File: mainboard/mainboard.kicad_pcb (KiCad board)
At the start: 2 copper layers, 94 parts, among them J1 CV-A, J2 In-A, J3 In-AB, J4 In-B, J5 Eurorack_Power, J6 CV-B, J7 Out-A, J8 Out-AB, J9 Out-B, Q1 BC547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

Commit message: Panel and trace corrections
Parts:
- added R50: 47k, Resistor_THT:R_Axial_DIN0204_L3.6mm_D1.6mm_P7.62mm_Horizontal, F.Cu at (68.5, 38.0)
- moved R37 174.9 mm to (18.5, 54.7), turned to -90 degrees
- moved R47 169.9 mm to (2.44, 39.8)
- moved R20 168.1 mm to (26.0, 54.7), turned to -90 degrees
- moved Q2 165.8 mm to (38.2, 34.0), turned to 90 degrees
- moved C9 165.1 mm to (39.2, 46.8), turned to 90 degrees
- moved Q4 162.0 mm to (32.2, 31.5), turned to -90 degrees
- moved R24 161.6 mm to (31.2, 39.5)
- moved R3 159.5 mm to (26.0, 20.0), turned to 180 degrees
- moved R26 159.4 mm to (18.4, 83.8)
- moved Q3 157.8 mm to (36.8, 17.0), turned to 90 degrees
- moved C10 155.2 mm to (40.8, 12.8), turned to -90 degrees
- moved R8 153.9 mm to (30.0, 20.5), turned to -90 degrees
- moved R30 153.5 mm to (30.0, 69.5), turned to 90 degrees
- moved C14 152.6 mm to (13.2, 86.8), turned to -90 degrees
- moved C6 149.6 mm to (39.2, 6.75), turned to 90 degrees
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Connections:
- R13 pad 2: Net-(R10-Pad1) -> Net-(R13-Pad2)
- R5 pad 2: Net-(R10-Pad1) -> Net-(R13-Pad2)
- R9 pad 1: Net-(R10-Pad1) -> Net-(R13-Pad2)
- U1 pad 2: unconnected-(U1-Pad2) -> GND
- U2 pad 12: MIDO1 -> Net-(RV3-Pad2)
- U2 pad 13: Net-(C10-Pad1) -> Net-(R13-Pad2)
- U2 pad 14: Net-(C10-Pad2) -> Net-(R13-Pad1)
- U2 pad 5: Net-(RV3-Pad2) -> MIDO1
- U2 pad 6: Net-(R10-Pad1) -> Net-(C10-Pad1)
- U2 pad 7: Net-(R13-Pad1) -> Net-(C10-Pad2)
- U3 pad 12: MIDO2 -> Net-(RV4-Pad2)
- U3 pad 13: Net-(C11-Pad1) -> Net-(R10-Pad1)
- U3 pad 14: Net-(C11-Pad2) -> Net-(R14-Pad1)
- U3 pad 5: Net-(RV4-Pad2) -> MIDO2
- U3 pad 6: Net-(R10-Pad1) -> Net-(C11-Pad1)
- U3 pad 7: Net-(R14-Pad1) -> Net-(C11-Pad2)
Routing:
- net GND: track 0.00 -> 463.9 mm, vias 0 -> 2
- net +9V: track 0.00 -> 297.5 mm, vias 0 -> 1
- net MIDO2: track 0.00 -> 101.9 mm, vias 0 -> 1
- net MIDO1: track 0.00 -> 98.1 mm
- net Net-(C11-Pad2): track 0.00 -> 93.9 mm, vias 0 -> 2
- net Net-(R16-Pad1): track 0.00 -> 93.5 mm
- net Net-(R33-Pad1): track 0.00 -> 77.2 mm
- net Net-(RV4-Pad2): track 0.00 -> 74.5 mm, vias 0 -> 1
- net Net-(C10-Pad2): track 0.00 -> 74.3 mm, vias 0 -> 1
- net Net-(C11-Pad1): track 0.00 -> 64.5 mm, vias 0 -> 1
- net Net-(C7-Pad1): track 0.00 -> 64.0 mm
- net Net-(R34-Pad1): track 0.00 -> 62.6 mm
- net Net-(C8-Pad1): track 0.00 -> 62.0 mm, vias 0 -> 1
- net Net-(R17-Pad1): track 0.00 -> 60.6 mm
- net Net-(C10-Pad1): track 0.00 -> 58.3 mm
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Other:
- board outline added: 70 x 100 mm
- board text added: "circuit: Ciat-Lonbarde pcb: Neil Massey"
- board text added: "panel components other side!"
- board text added: "panel components this side!"
- board text added: "thanks: Josh Rodriguez, T.Johns"

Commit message: Panel tweaks
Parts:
- moved J1 0.25 mm to (64.0, 28.5)
- moved J2 0.25 mm to (64.0, 6.50)
- moved J3 0.25 mm to (64.0, 50.0)
- moved J4 0.25 mm to (64.0, 91.0)
- moved J6 0.25 mm to (64.0, 70.5)
- moved J7 0.25 mm to (6.00, 6.50)
- moved J8 0.25 mm to (6.00, 50.0)
- moved J9 0.25 mm to (6.00, 91.0)
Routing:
- net GND: track 463.9 -> 464.5 mm

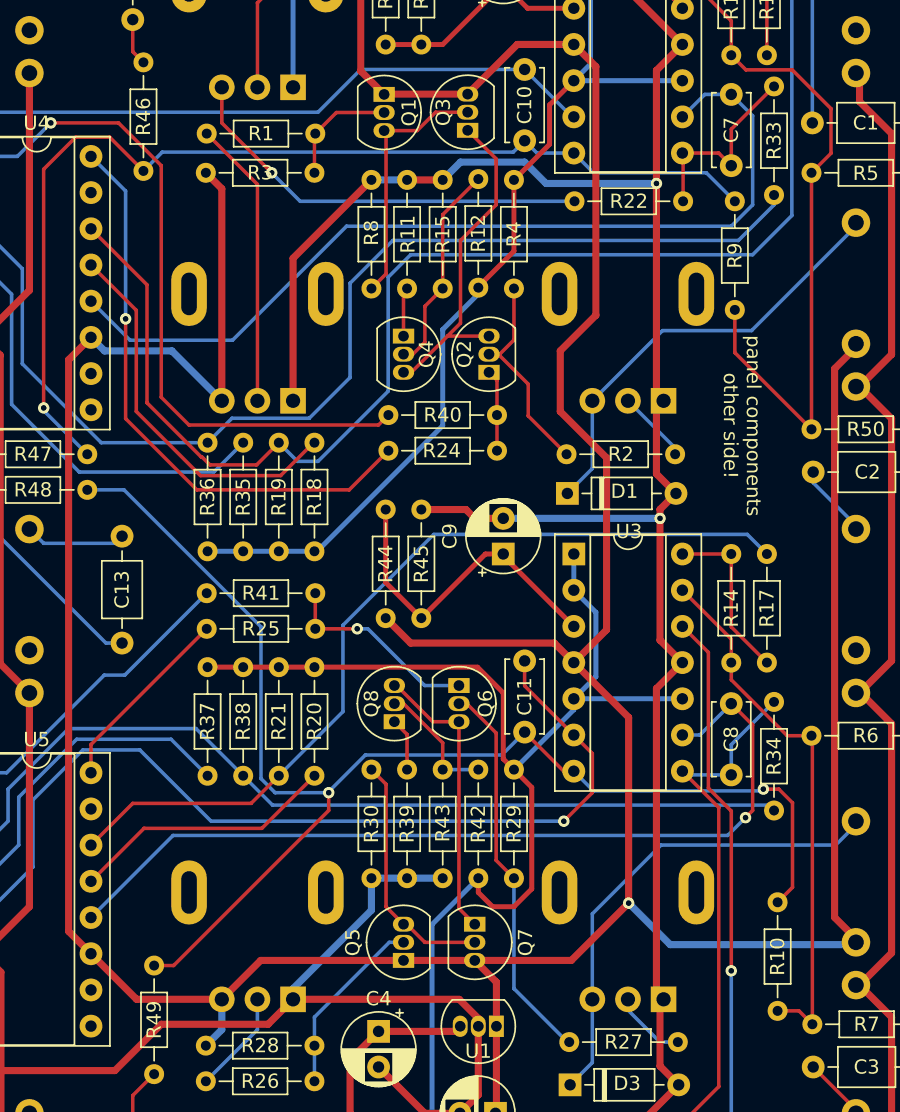
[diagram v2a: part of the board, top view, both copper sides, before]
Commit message: updated BOM, some layout tweaks
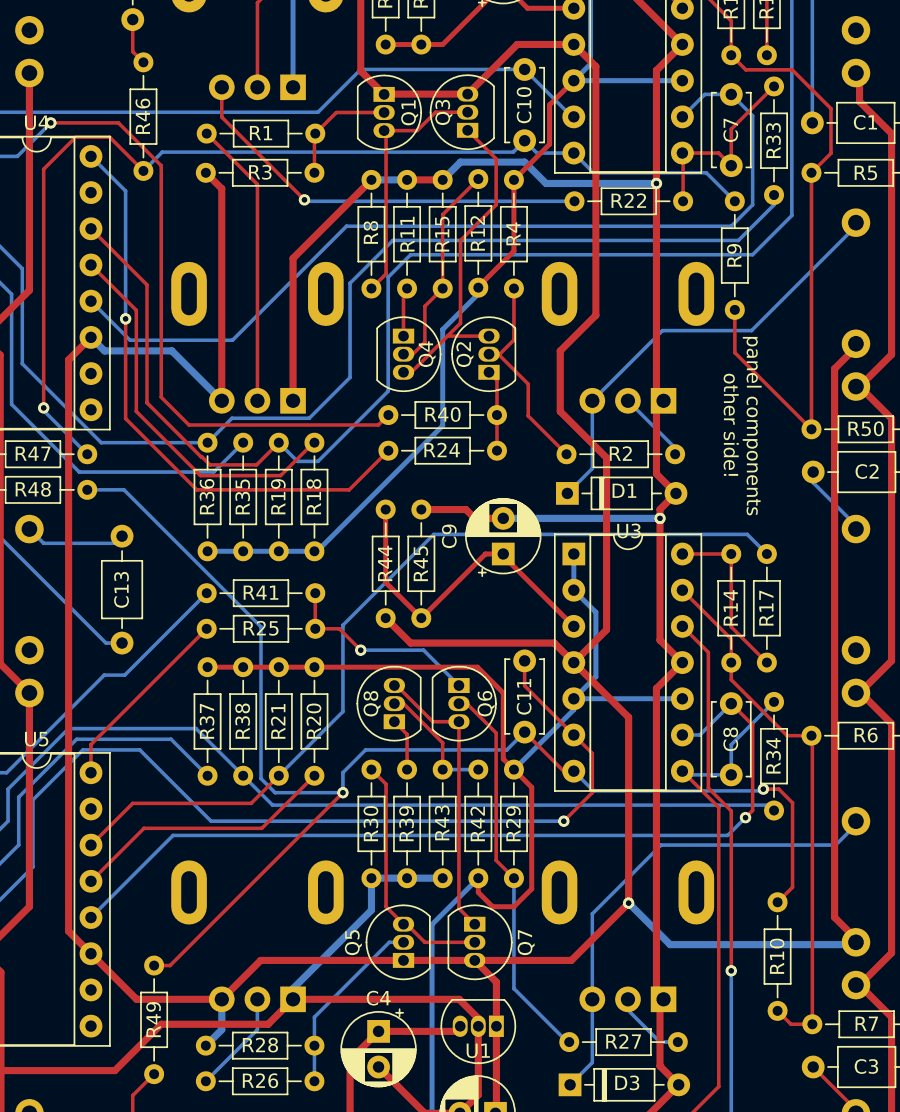
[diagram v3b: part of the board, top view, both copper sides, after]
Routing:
- net Net-(C11-Pad2): track 93.9 -> 95.0 mm
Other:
- board text added: "thanks: Josh Rodriguez, T. Johns"
- board text removed: "thanks: Josh Rodriguez, T.Johns"
